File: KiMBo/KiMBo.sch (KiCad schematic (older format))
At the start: 74 parts, among them CON1 μSD, P1 BED_THERM, P10 ENC, P11 Serial, P12 μUSB, P13 USB_Type_A, P14 Ethernet, P15 JTAG, P16 E_MOTOR, P17 H_MOTOR, P18 X0_MOTOR, P19 X1_MOTOR, P2 ADC, P20 Y0_MOTOR, P21 Y1_MOTOR, P22 Z0_MOTOR, P23 Z1_MOTOR, P24 Z2_MOTOR, P25 BED_HEAT, P26 E_HEAT, P27 H_HEAT, P28 DOCK0_HEAT, P29 DOCK1_HEAT, P3 TOOLHEAD0, P30 E_FAN, P31 H_FAN, P32 PWM, P33 CASE_FAN, P34 HS_FAN, P4 TOOLHEAD1, P5 DOCK0, P6 DOCK1, P7 X1, P8 Y2, P9 Z1, U1 MAX3370, X1 HDMI

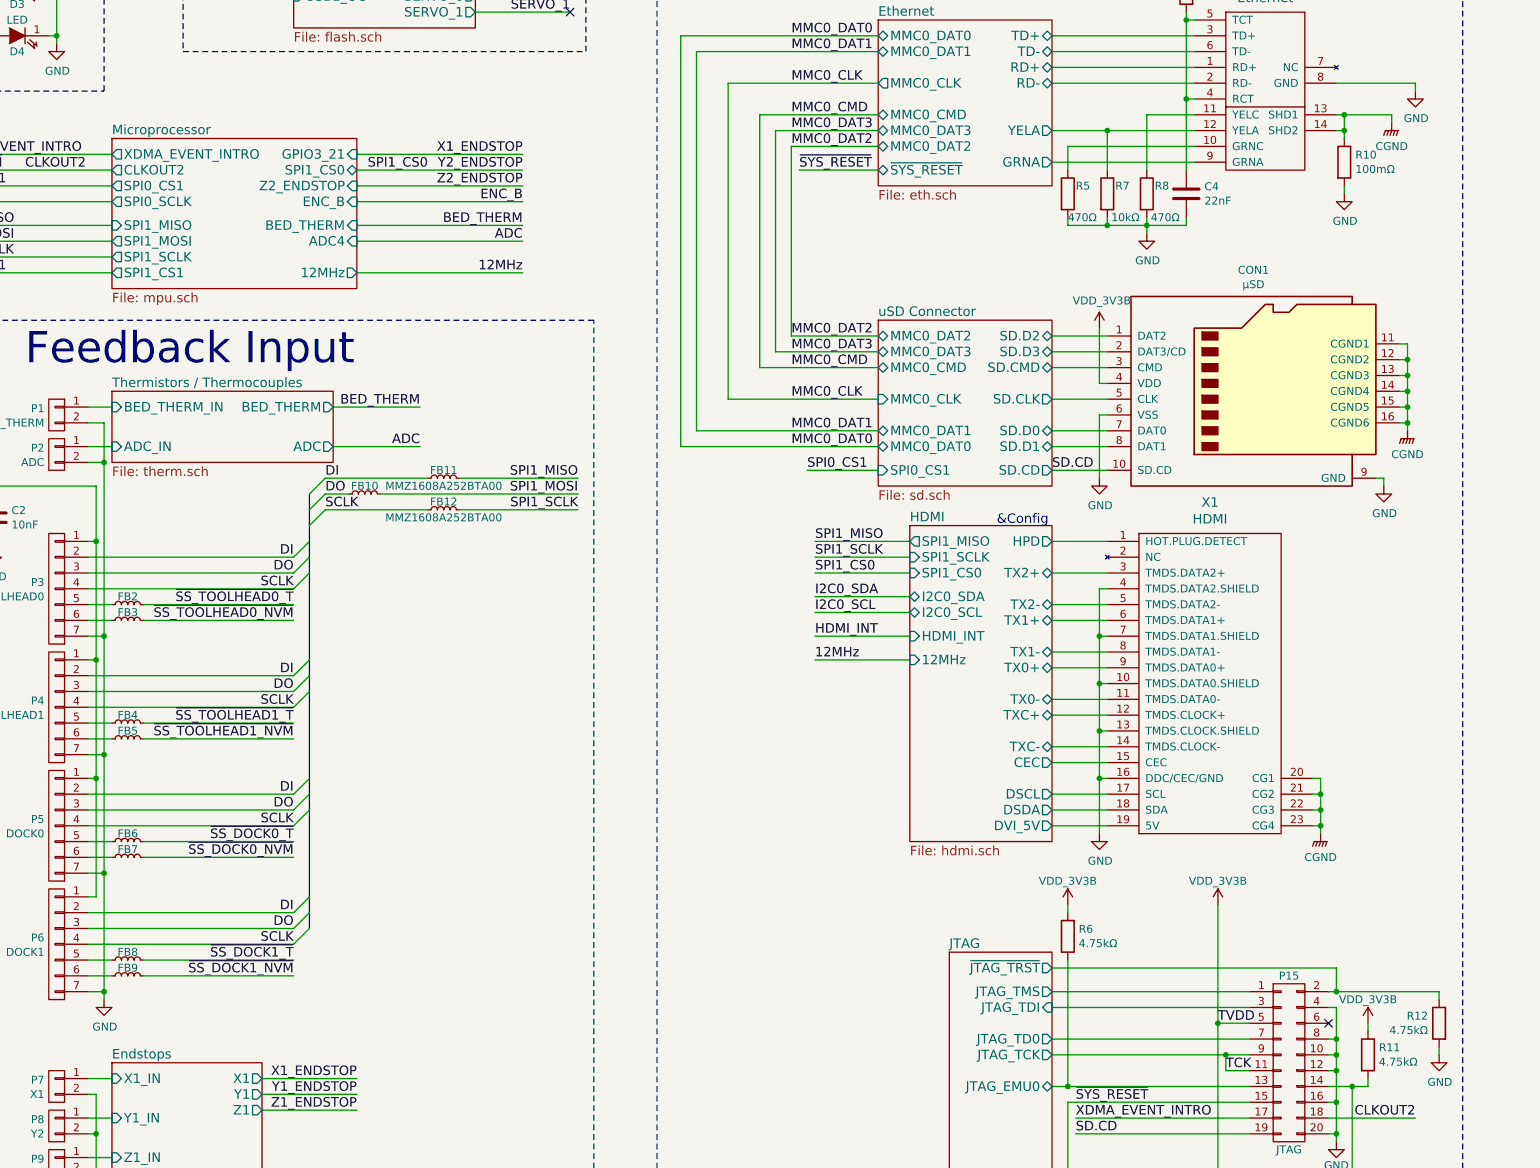
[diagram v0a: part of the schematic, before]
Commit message: Add equivalent annotations document, associate more footprints
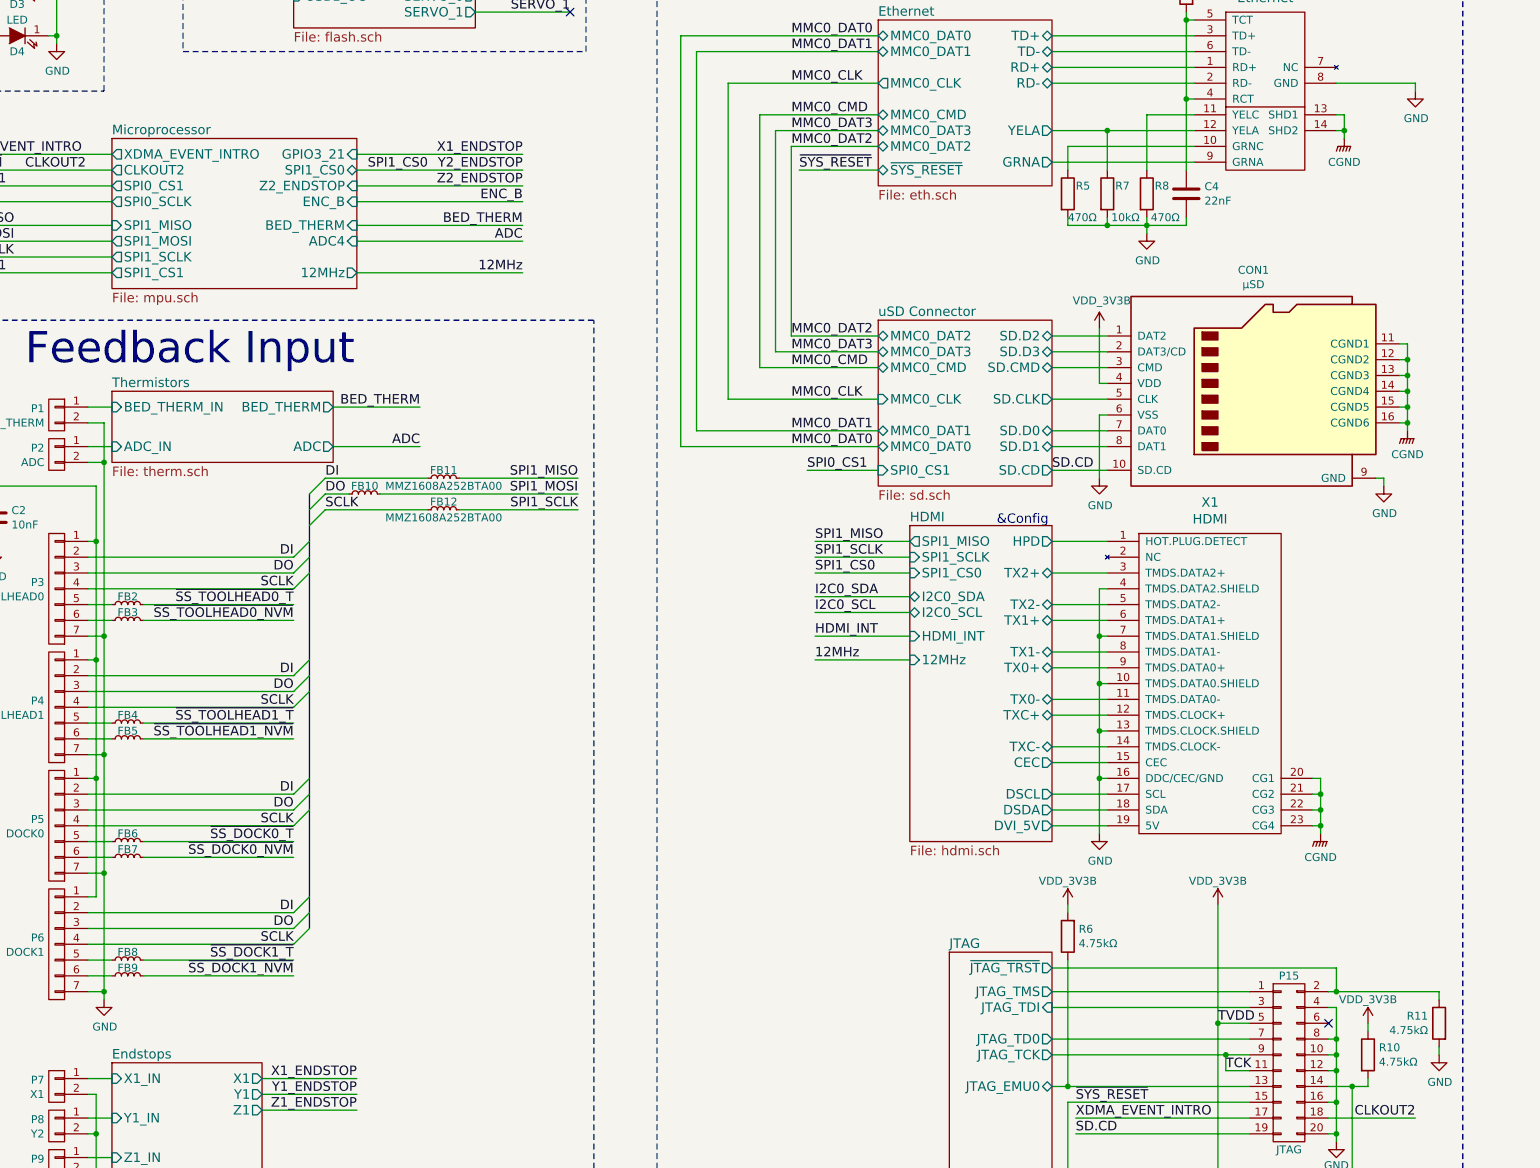
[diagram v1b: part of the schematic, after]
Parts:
- removed R10: 100mΩ, symbol R
- C3, C4, C5: footprint (none) -> Capacitors_SMD:C_0402
- R1, R2, R3, R4, R5, R6, R7, R8, R9: footprint (none) -> Resistors_SMD:R_0402
- R10: renamed from R11; footprint (none) -> Resistors_SMD:R_0402
- R11: renamed from R12; footprint (none) -> Resistors_SMD:R_0402
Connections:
- wire segments 410 -> 408

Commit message: Change the endstop RC filter
Lower the time constant

Reduce the series resistor to 100Ohms
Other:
- note added: "maybe use a buffer stage instead"
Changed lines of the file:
@@
 	10050 3700 10050 3850
 Connection ~ 10050 3800
+Text Notes 12100 2150 0    60   ~ 0
+maybe use a buffer stage instead
 $EndSCHEMATC

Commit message: Leave SPI0 free for a display, reassign pins so SPI1 is available
Fix some typos/errors
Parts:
- removed U1: MAX3370, symbol MAX3370
- added Q1: 2N7002, symbol 2N7002P,215
- added R12, R13: 4.7kΩ, Resistors_SMD:R_0402, symbol R
- renumbered P32 to P16, P16 to P17, P17 to P18, P18 to P19, P19 to P20, P20 to P21, P21 to P22, P22 to P23, P23 to P24, P24 to P25, P25 to P26, P26 to P27, P27 to P28, P28 to P29, P29 to P30, P30 to P31, P31 to P32
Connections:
- net labels added: SPI0_CS0, SPI0_MISO, SPI0_MOSI, SPI0_SCLK, ~DISP_INT
- wire segments 408 -> 414
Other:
- note added: "Available"
- note added: "HDMI"
- note added: "High-Z Input?"
- note added: "Steppers"
- note added: "Unused on BBB"
- note added: "uSD"
- note removed: "may be unneeded"
- note removed: "maybe use a buffer stage instead"
- moved on the sheet: D5, FB13, FB14, P16

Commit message: Use fixed 5V LM2592HV Buck, include SPI0 header for LCD
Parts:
- added FB13, FB14, FB15, FB16, FB17: MMZ1608A252BTA00, symbol INDUCTOR_Small
- added P16: DISPLAY, symbol CONN_01X07
- FB1: value MMZ1608A252BTA00 -> MPZ1608S102ATA00
- FB18: renamed from FB13; value MMZ1608A252BTA00 -> MPZ1608S102ATA00
- renumbered FB14 to FB19, FB15 to FB20, P16 to P17, P17 to P18, P18 to P19, P19 to P20, P20 to P21, P21 to P22, P22 to P23, P23 to P24, P24 to P25, P25 to P26, P26 to P27, P27 to P28, P28 to P29, P29 to P30, P30 to P31, P31 to P32, P32 to P33, P33 to P34, P34 to P35
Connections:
- net DI: now also FB10.1, P3.3 (P3); no longer FB11.1, P3.2 (P2)
- net DO: now also FB12.1, P3.4 (P4); no longer FB10.1, P3.3 (P3)
- net GND: now also P16.7 (P7)
- net SCLK: now also FB11.1, P3.2 (P2); no longer FB12.1, P3.4 (P4)
- net SPI0_CS0: now also FB16.1
- net SPI0_MISO: now also FB14.1
- net SPI0_MOSI: now also FB15.1
- net SPI0_SCLK: now also FB13.1
- net SPI1_MISO: now also FB10.2; no longer FB11.2
- net SPI1_MOSI: now also FB12.2; no longer FB10.2
- net SPI1_SCLK: now also FB11.2; no longer FB12.2
- net ~DISP_INT: now also FB17.1
- net 3V3_FILTERED: now reaches C1.1, C2.1, FB1.1, P3.1 (P1), P4.1 (P1), P5.1 (P1), P6.1 (P1)
- net 3V3_FILTERED: now also P16.1 (P1)
- new net: FB13.2, P16.2 (P2)
- new net: FB14.2, P16.3 (P3)
- new net: FB15.2, P16.4 (P4)
- new net: FB16.2, P16.5 (P5)
- new net: FB17.2, P16.6 (P6)
- no-connect marks 2 -> 1
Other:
- note added: "Unused on BBBW"
- note removed: "High-Z Input?"
- note removed: "Unused on BBB"

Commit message: Assocate more footprints
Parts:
- added D6: D5V0F1U2S9, symbol ZENER
- C1, C2, C3, C4, C5: footprint Capacitors_SMD:C_0402 -> Capacitors_SMD:C_0603
- D1, D2, D3, D4: footprint (none) -> LEDs:LED_0603
- FB1, FB10, FB11, FB12, FB13, FB14, FB15, FB16, FB17, FB18, FB19, FB2, FB3, FB4, FB5, FB6, FB7, FB8, FB9: footprint (none) -> KiMBo:Ferrite_Bead_0603
- FB20: value MMZ1608A252BTA00 -> MPZ1608S102ATA00; footprint (none) -> KiMBo:Ferrite_Bead_0603
- P1, P10, P2, P35, P7, P8, P9: footprint (none) -> Pin_Headers:Pin_Header_Angled_1x02
- P16: value DISPLAY -> LCD; footprint (none) -> Pin_Headers:Pin_Header_Angled_1x07
- P17: renamed from P18; footprint (none) -> Pin_Headers:Pin_Header_Angled_1x04
- P18: renamed from P19; footprint (none) -> Pin_Headers:Pin_Header_Angled_1x04
- P19: renamed from P20; footprint (none) -> Pin_Headers:Pin_Header_Angled_1x04
- P20: renamed from P21; footprint (none) -> Pin_Headers:Pin_Header_Angled_1x04
- P21: renamed from P22; footprint (none) -> Pin_Headers:Pin_Header_Angled_1x04
- P22: renamed from P23; footprint (none) -> Pin_Headers:Pin_Header_Angled_1x04
- P23: renamed from P24; footprint (none) -> Pin_Headers:Pin_Header_Angled_1x04
- P24: renamed from P25; footprint (none) -> Pin_Headers:Pin_Header_Angled_1x04
- P25: renamed from P26; footprint (none) -> Pin_Headers:Pin_Header_Angled_1x04
- P3, P4, P5, P6: footprint (none) -> Pin_Headers:Pin_Header_Angled_1x07
- P31: renamed from P32; footprint (none) -> Pin_Headers:Pin_Header_Angled_1x02
- P32: renamed from P33; footprint (none) -> Pin_Headers:Pin_Header_Angled_1x02
- P33: renamed from P34; footprint (none) -> Pin_Headers:Pin_Header_Angled_1x02
- P34: renamed from P17; footprint (none) -> Pin_Headers:Pin_Header_Angled_1x03
- R1, R10, R11, R12, R13, R2, R3, R4, R5, R6, R7, R8, R9: footprint Resistors_SMD:R_0402 -> Resistors_SMD:R_0603
- renumbered P27 to P26, P28 to P27, P29 to P28, P30 to P29, P31 to P30
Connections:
- net GND: now also D6.2 (A)
- net VDD_5V: now also D6.1 (K)
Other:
- moved on the sheet: D5, FB18, FB19, P34, Q1, R12, R13

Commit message: More footprint association
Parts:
- added D5: TPD1E04U04DPYR, KiMBo:TPD_PX1SON, symbol ZENER
- D6: renamed from D5; footprint (none) -> KiMBo:SOD-923
- D7: renamed from D6; footprint (none) -> KiMBo:SOD-923
- P11: footprint (none) -> Pin_Headers:Pin_Header_Straight_1x03
- P26, P27, P28, P29, P30: footprint (none) -> KiMBo:euro_header_2_angled
- P8: value Y2 -> Y1
- Q1: footprint (none) -> TO_SOT_Packages_SMD:SOT-23
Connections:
- net 3V3_FILTERED: now also D5.1 (K)
- net GND: now also D5.2 (A)
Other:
- note added: "39532-1002"
- note added: "4.2x2.1 mm"
- note added: "LCD"
- note added: "μSD"
- note removed: "Available"
- note removed: "uSD"
- moved on the sheet: C1, C2, FB1, FB10, FB11, FB12, FB2, FB3, FB4, FB5, FB6, FB7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

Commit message: Create more footprints and add more associations
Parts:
- P12: footprint (none) -> KiMBo:USB_MICRO_B_ST-USB-001E
- P15: renamed from CON1; footprint (none) -> KiMBo:SCHA5B0200
- renumbered X1 to P14, P14 to P16, P15 to P17, P16 to P18, P17 to P19, P18 to P20, P19 to P21, P20 to P22, P21 to P23, P22 to P24, P23 to P25, P24 to P26, P25 to P27, P26 to P28, P27 to P29, P28 to P30, P29 to P31, P30 to P32, P31 to P33, P32 to P34, P33 to P35, P34 to P36, P35 to P37
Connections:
- net GND: now also P12.10, P12.11, P12.6, P12.7, P12.8, P12.9
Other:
- note added: "Shift Registers"
- note removed: "Steppers"
- moved on the sheet: FB13, FB14, FB15, FB16, FB17, P18

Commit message: Add more footprints and more associations, one association left!
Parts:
- P13: footprint (none) -> Connectors:USB_A
- P14: footprint (none) -> KiMBo:MICRO-HDMI-D
- P16: footprint (none) -> KiMBo:Ethernet-LPJ0011BBNL
- P17: footprint (none) -> KiMBo:JTAG
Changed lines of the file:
@@
 F 0 "P13" H 8700 2300 50  0000 L CNN
 F 1 "USB_Type_A" V 9050 1825 50  0000 L CNN
-F 2 "" V 8800 1950 50  0001 C CNN
+F 2 "Connectors:USB_A" V 8800 1950 50  0001 C CNN
 F 3 "" V 8800 1950 50  0000 C CNN
 	1    8800 2050
@@
 F 0 "P14" H 9200 8447 60  0000 C CNN
 F 1 "HDMI" H 9200 8341 60  0000 C CNN
-F 2 "" H 9250 7450 60  0001 C CNN
+F 2 "KiMBo:MICRO-HDMI-D" H 9250 7450 60  0001 C CNN
 F 3 "http://media.digikey.com/pdf/Data%20Sheets/FCI%20PDFs/10118241-001RLF_Webpage.PDF" H 9250 7450 60  0001 C CNN
 	1    9200 7300
@@
 F 0 "P16" H 9550 4247 60  0000 C CNN
 F 1 "Ethernet" H 9550 4141 60  0000 C CNN
-F 2 "" H 9550 4150 60  0001 C CNN
+F 2 "KiMBo:Ethernet-LPJ0011BBNL" H 9550 4150 60  0001 C CNN
 F 3 "http://www.link-pp.com/?product/201411246424.html" H 9550 4150 60  0001 C CNN
 	1    9550 3550
@@
 F 0 "P17" H 9700 10250 50  0000 C CNN
 F 1 "JTAG" H 9700 9150 50  0000 C CNN
-F 2 "" H 9700 8500 50  0001 C CNN
+F 2 "KiMBo:JTAG" H 9700 8500 50  0001 C CNN
 F 3 "" H 9700 8500 50  0000 C CNN
 	1    9700 9700
